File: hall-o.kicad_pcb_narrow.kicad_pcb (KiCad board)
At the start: 2 copper layers, 44.2 x 17.8 mm, 16 parts, among them P1 CONN_01X04, Q1 BC848, U1 ss495b, U2 LM258D

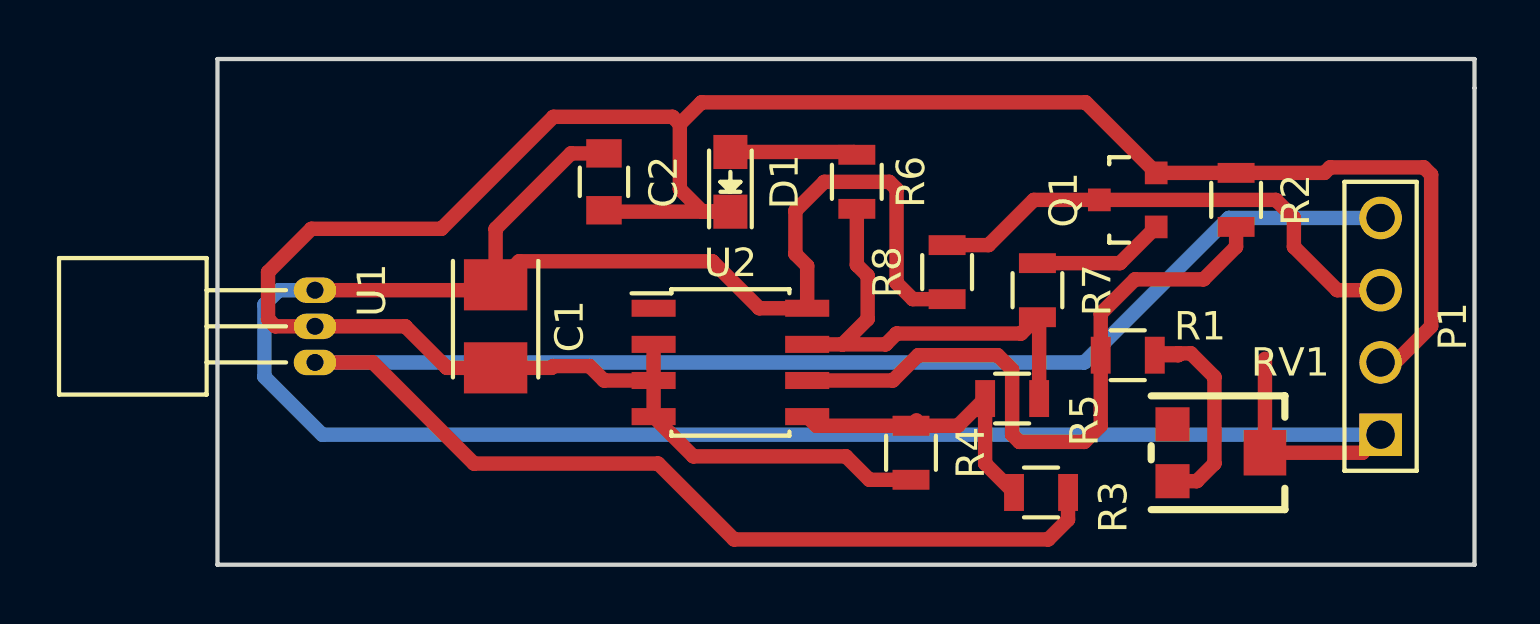
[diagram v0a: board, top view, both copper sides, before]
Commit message: thickened traces
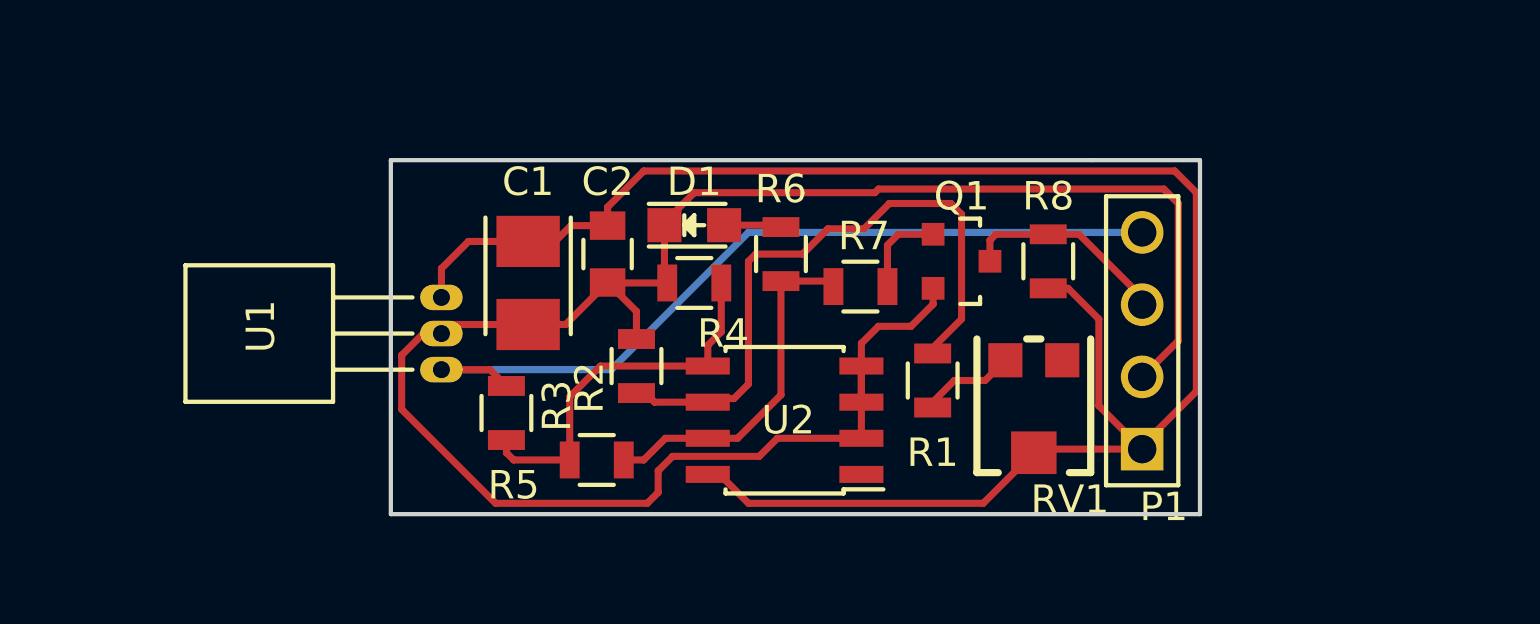
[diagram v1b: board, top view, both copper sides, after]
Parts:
- moved R2 21.9 mm to (132.6, 104.3)
- moved R3 19.0 mm to (128.0, 105.9), turned to 270 degrees
- moved R5 14.8 mm to (131.2, 107.6)
- moved R4 9.68 mm to (134.6, 101.3), turned to 180 degrees
- moved P1 8.40 mm to (150.4, 103.4)
- moved R1 6.92 mm to (143.0, 104.8), turned to 270 degrees
- moved RV1 6.68 mm to (146.6, 105.7), turned to 180 degrees
- moved Q1 6.23 mm to (144.0, 100.6), turned to 270 degrees
- moved R7 6.22 mm to (140.5, 101.5), turned to 180 degrees
- moved U1 4.45 mm to (125.7, 101.9)
- moved R6 3.68 mm to (137.7, 100.3)
- moved R8 3.58 mm to (147.1, 100.6)
- moved U2 2.79 mm to (137.8, 106.2), turned to 180 degrees
- moved C2 2.54 mm to (131.6, 100.3)
- moved D1 1.98 mm to (134.6, 99.3), turned to 0 degrees
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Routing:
- net /SIG: track 69.9 -> 29.2 mm
- net /+5V: track 90.5 -> 63.6 mm
- net /GND: track 89.9 -> 70.0 mm
- net /STOP: track 17.8 -> 7.35 mm
- net Net-(R1-Pad2): track 7.79 -> 3.35 mm
- net Net-(R5-Pad1): track 16.7 -> 12.7 mm
- net Net-(R3-Pad2): track 10.8 -> 13.4 mm
- net Net-(D1-Pad2): track 4.49 -> 2.03 mm
- net Net-(Q1-Pad1): track 4.70 -> 3.22 mm
- net Net-(R1-Pad1): track 23.9 -> 22.5 mm
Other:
- board size 44.2 x 17.8 mm -> 28.4 x 12.4 mm
